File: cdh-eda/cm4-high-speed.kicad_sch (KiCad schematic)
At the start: 7 parts, among them J4 USB_OTG, U2 TPD2EUSB30ADRTR

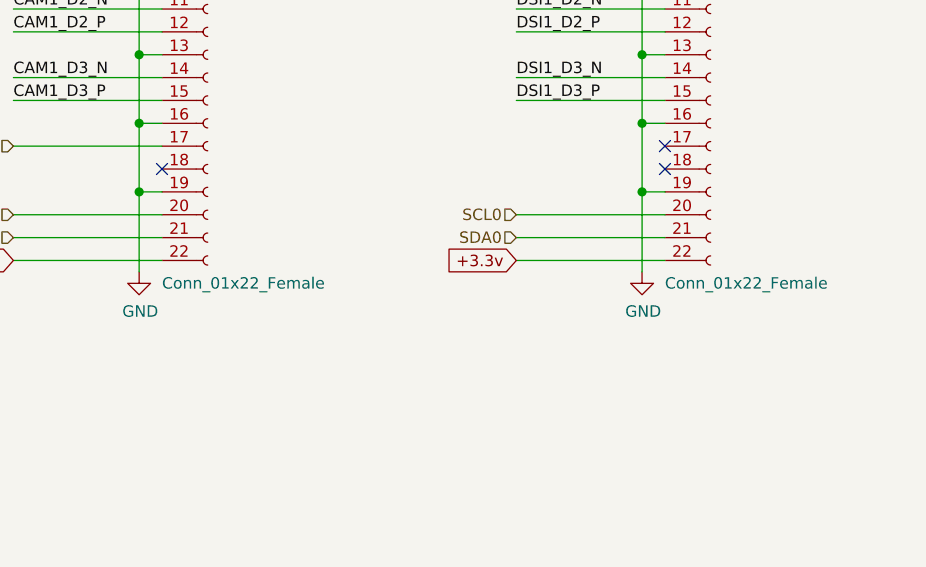
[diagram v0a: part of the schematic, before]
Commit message: v.2 updates
created separate BOMS for JCLPCB and In house purchases
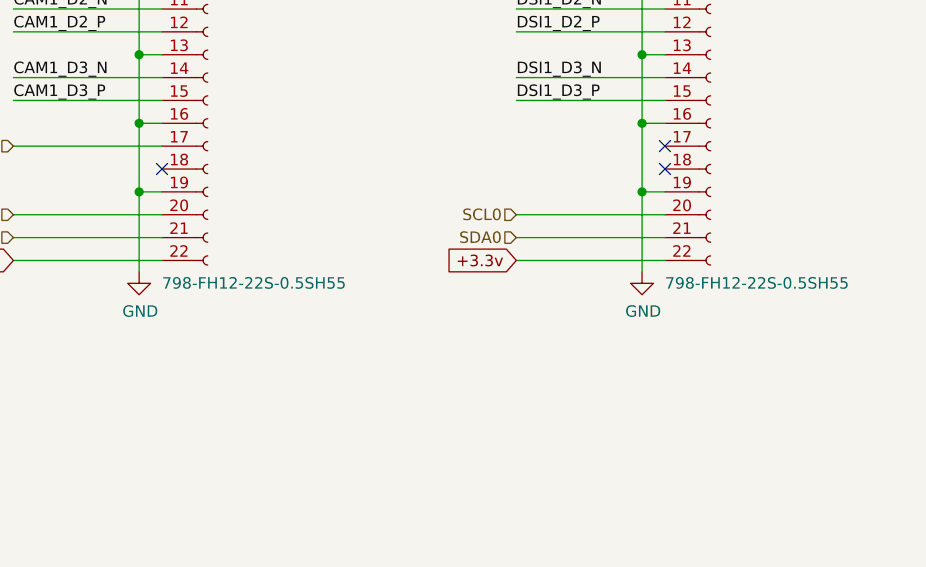
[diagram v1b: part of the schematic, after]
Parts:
- Camera1, Display1: value Conn_01x22_Female -> 798-FH12-22S-0.5SH55
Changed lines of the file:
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@@
       (effects (font (size 1.27 1.27)) (justify left))
     )
-    (property "Value" "Conn_01x22_Female" (id 1) (at 218.44 149.86 0)
+    (property "Value" "798-FH12-22S-0.5SH55" (id 1) (at 218.44 149.86 0)
       (effects (font (size 1.27 1.27)) (justify left))
     )
@@
       (effects (font (size 1.27 1.27)) (justify left))
     )
-    (property "Value" "Conn_01x22_Female" (id 1) (at 162.56 149.86 0)
-      (effects (font (size 1.27 1.27)) (justify left))
-    )
+    (property "Value" "798-FH12-22S-0.5SH55" (id 1) (at 162.56 149.86 0)
+      (effects (font (size 1.27 1.27)) (justify left))
+    )
